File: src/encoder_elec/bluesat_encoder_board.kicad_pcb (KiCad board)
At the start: 2 copper layers, 30 x 23 mm, 5 parts, among them J1 SM06B-PASS, U1 AS5047D

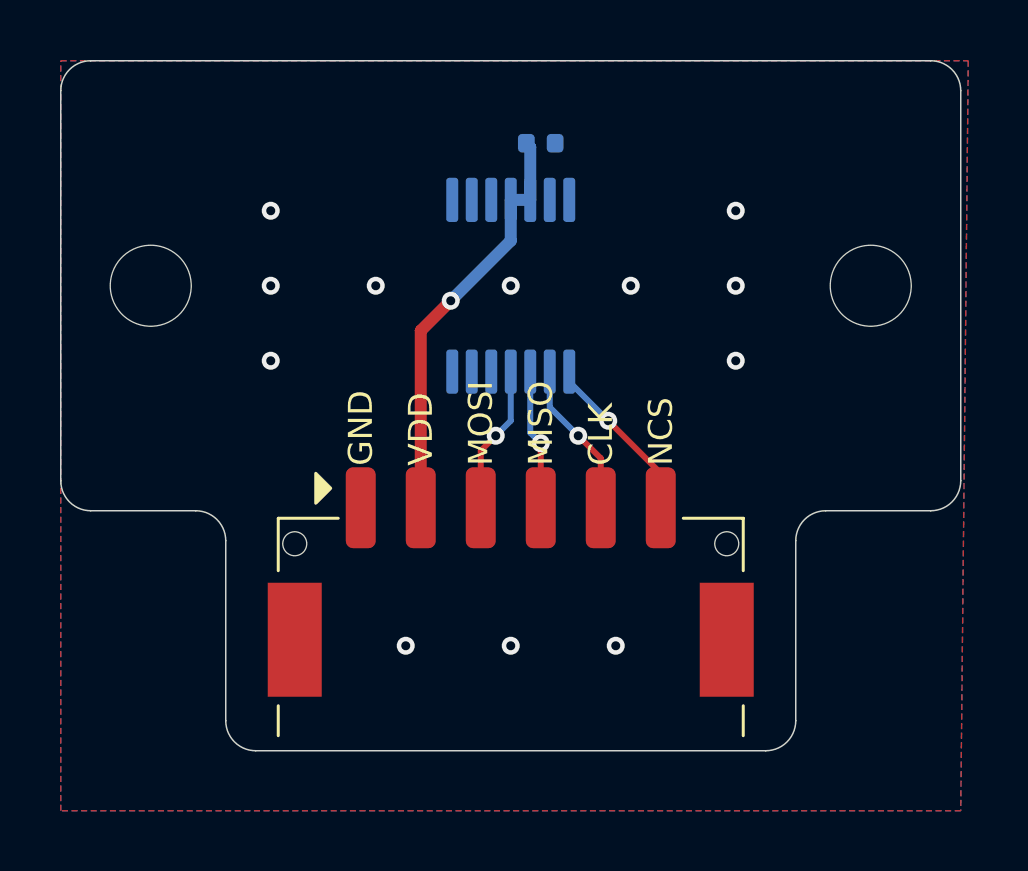
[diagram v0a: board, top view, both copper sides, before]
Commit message: [ELEC] REV markers on all PCB's, Fix USB hub passives
Add mounting holes to all PCB schematics
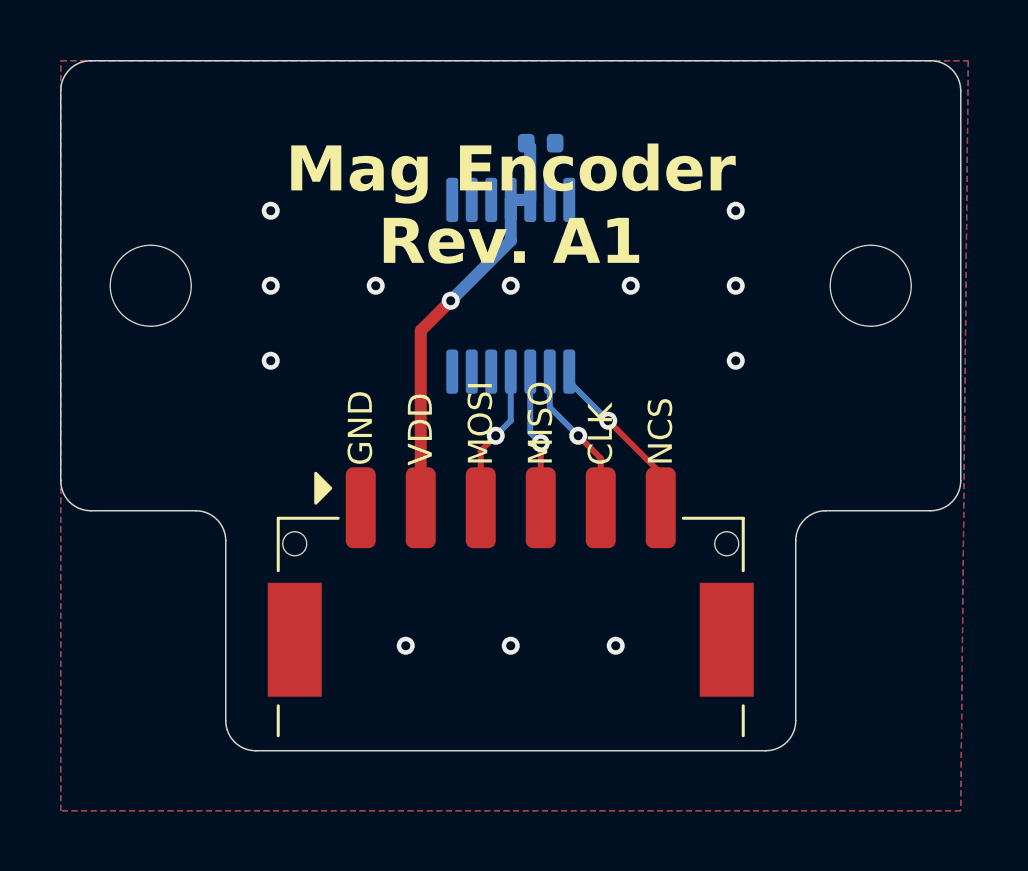
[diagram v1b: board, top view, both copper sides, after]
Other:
- board text added: "Mag Encoder Rev. A1"
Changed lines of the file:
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@@
 		(tenting front back)
 		(pcbplotparams
-			(layerselection 0x00000000_00000000_55555555_5755f5ff)
+			(layerselection 0x00000000_00000000_55555555_5555f551)
 			(plot_on_all_layers_selection 0x00000000_00000000_00000000_00000000)
 			(disableapertmacros no)
@@
 			(crossoutdnponfab yes)
 			(subtractmaskfromsilk no)
-			(outputformat 1)
+			(outputformat 5)
 			(mirror no)
-			(drillshape 1)
+			(drillshape 0)
 			(scaleselection 1)
 			(outputdirectory "")
@@
 			(unlocked yes)
 			(layer "F.Fab")
+			(hide yes)
 			(effects
 				(font
@@
 		(sheetfile "bluesat_encoder_board.kicad_sch")
 		(attr smd exclude_from_bom)
-		(fp_text user "${REFERENCE}"
-			(at 0 2.5 0)
-			(unlocked yes)
-			(layer "F.Fab")
-			(effects
-				(font
-					(size 1 1)
-					(thickness 0.15)
-				)
-			)
-		)
 		(pad "" np_thru_hole circle
 			(at 2.5 0.75)
@@
 			(unlocked yes)
 			(layer "F.Fab")
+			(hide yes)
 			(effects
 				(font
@@
 		(sheetfile "bluesat_encoder_board.kicad_sch")
 		(attr smd exclude_from_bom)
-		(fp_text user "${REFERENCE}"
-			(at 0 2.5 0)
-			(unlocked yes)
-			(layer "F.Fab")
-			(effects
-				(font
-					(size 1 1)
-					(thickness 0.15)
-				)
-			)
-		)
 		(pad "" np_thru_hole circle
 			(at -3.25 0)
@@
 		)
 	)
+	(gr_text "Mag Encoder\nRev. A1"
+		(at 0 -4.75 0)
+		(layer "F.SilkS")
+		(effects
+			(font
+				(size 1.5 1.5)
+				(thickness 0.3)
+				(bold yes)
+			)
+			(justify top)
+		)
+	)
